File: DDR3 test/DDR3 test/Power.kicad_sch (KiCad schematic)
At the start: 24 parts, among them U1 MPM3834CGPA-Z, U2 MPM3834CGPA-Z, U4 TPS3106K33DBVR

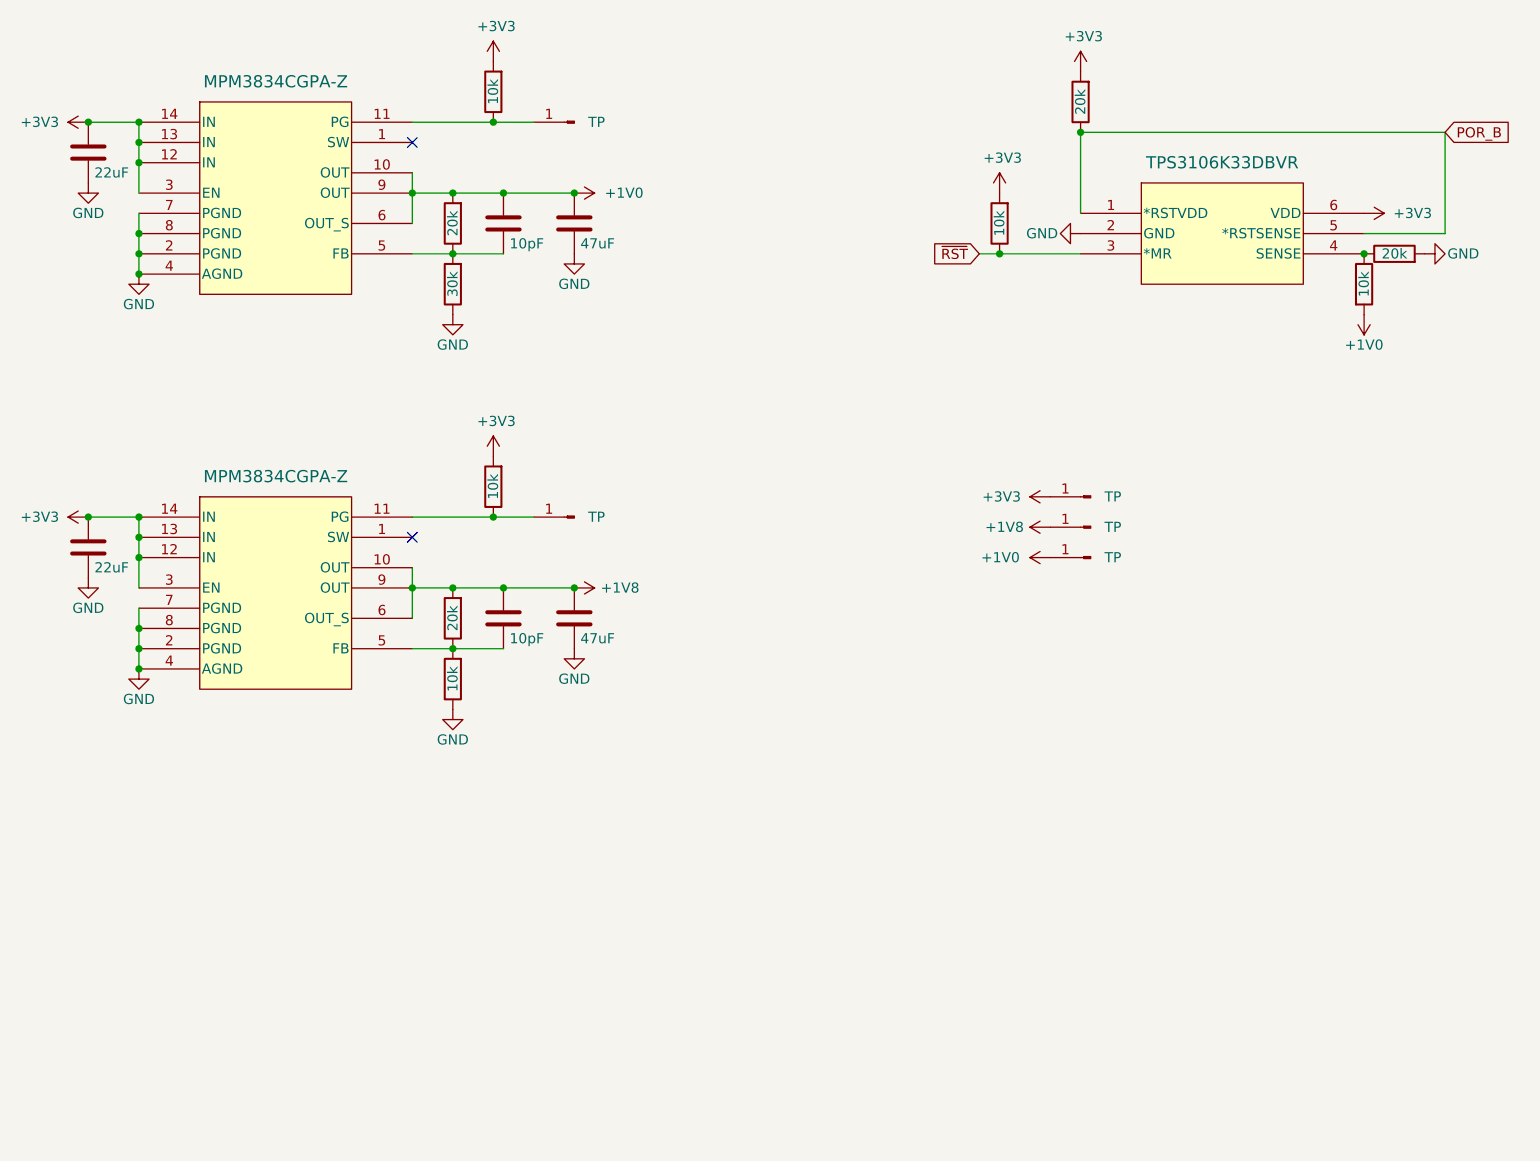
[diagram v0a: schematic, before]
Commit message: group ddr pins by function in symbol
group ddr pins by function in symbol
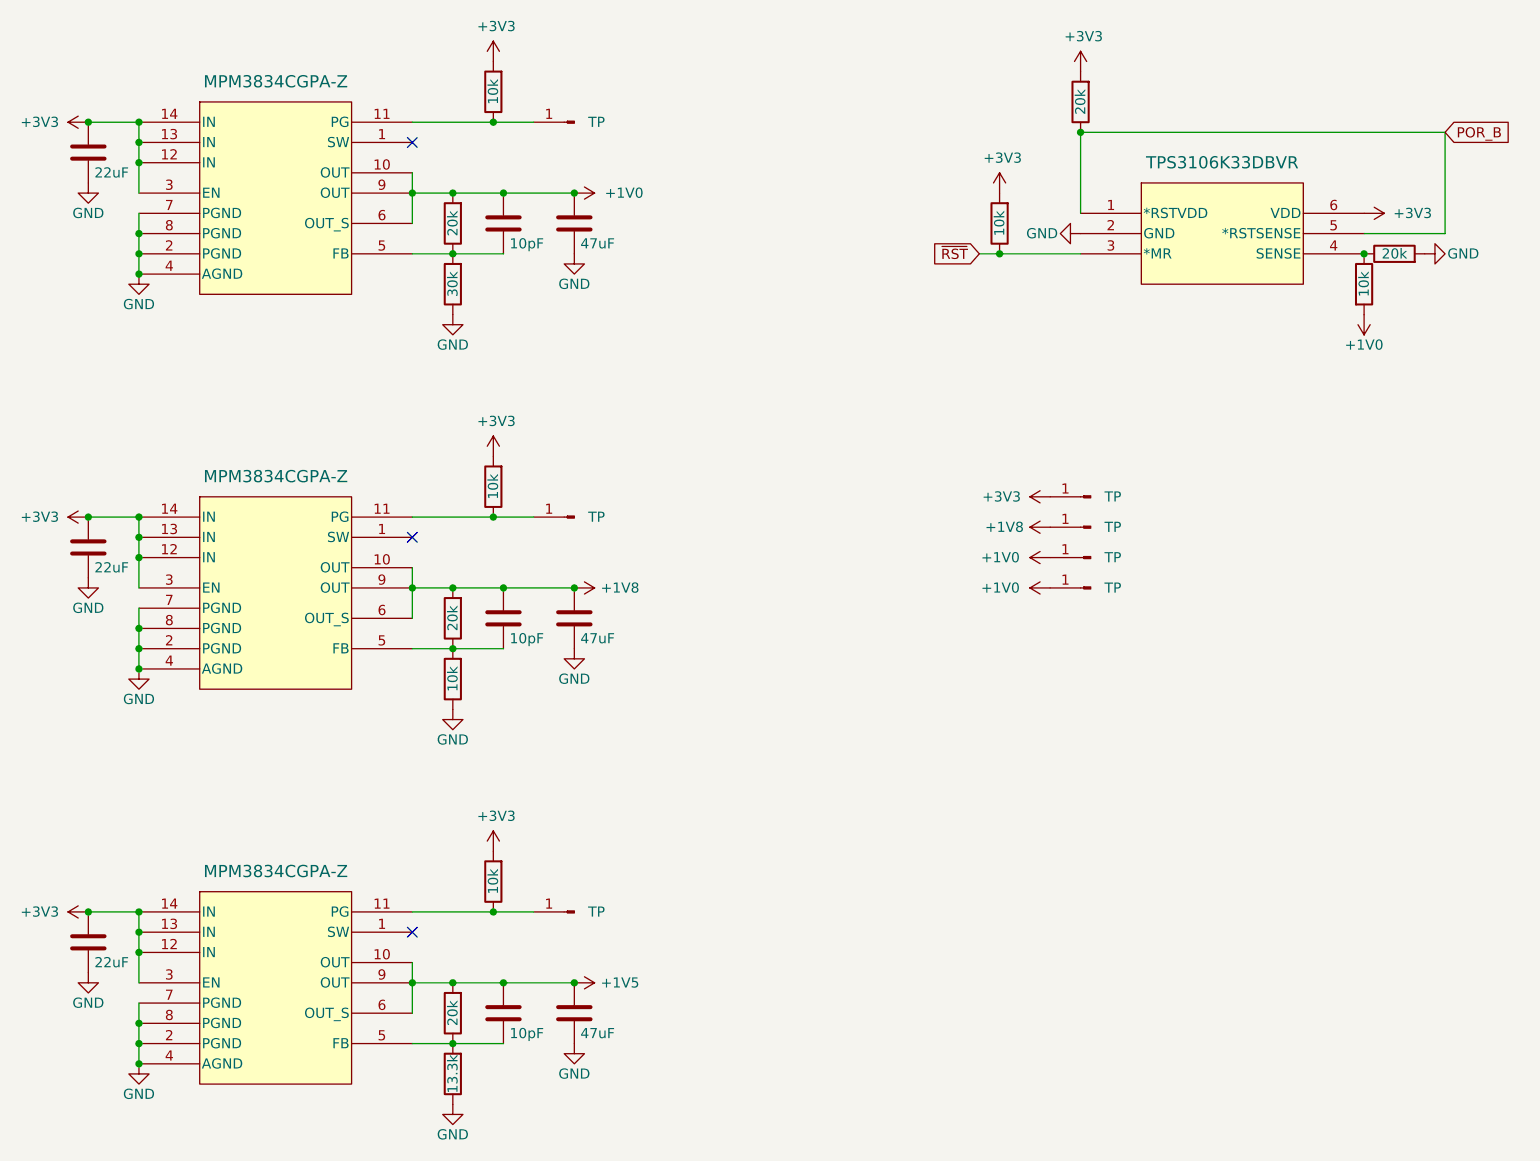
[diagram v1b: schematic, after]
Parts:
- added C2: 22uF, Capacitor_SMD:C_0402_1005Metric, symbol Device:C
- added C3: 10pF, Capacitor_SMD:C_0201_0603Metric, symbol Device:C
- added C4: 47uF, Capacitor_SMD:C_0805_2012Metric, symbol Device:C
- added R29: 20k, Capacitor_SMD:C_0201_0603Metric, symbol Device:R
- added R30: 13.3k, Capacitor_SMD:C_0402_1005Metric, symbol Device:R
- added R31: 10k, Capacitor_SMD:C_0402_1005Metric, symbol Device:R
- added TP6, TP7: TP, TestPoint:TestPoint_Pad_1.0x1.0mm, symbol Connector:Conn_01x01_Pin
- added U8: MPM3834CGPA-Z, Sync_VT extras:ECLGA-14_MPM3834C_MNP, symbol Personal:MPM3834CGPA-Z
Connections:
- net +1V0: now also TP7.1 (Pin_1)
- net +3V3: now also C2.1, R31.2, U8.12 (IN), U8.13 (IN), U8.14 (IN), U8.3 (EN)
- net GND: now also C2.2, C4.2, R30.1, U8.2 (PGND), U8.4 (AGND), U8.7 (PGND), U8.8 (PGND)
- new net: C3.2, R29.1, R30.2, U8.5 (FB)
- new net: R31.1, TP6.1 (Pin_1), U8.11 (PG)
- new net +1V5: C3.1, C4.1, R29.2, U8.10 (OUT), U8.6 (OUT_S), U8.9 (OUT)
- no-connect marks 2 -> 3

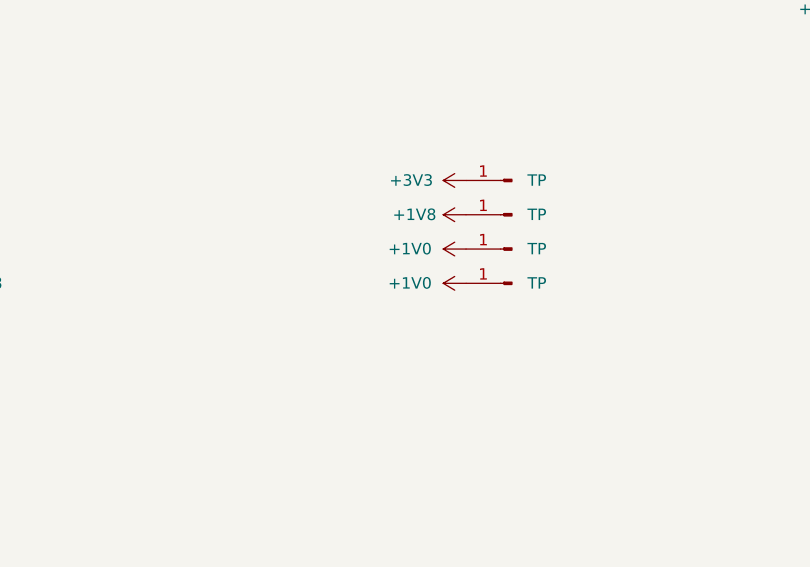
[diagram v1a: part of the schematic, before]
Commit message: Resistor Footprints
- Fixed resistor footprints
- Re-added 3D models
- Routed 1.5V reg
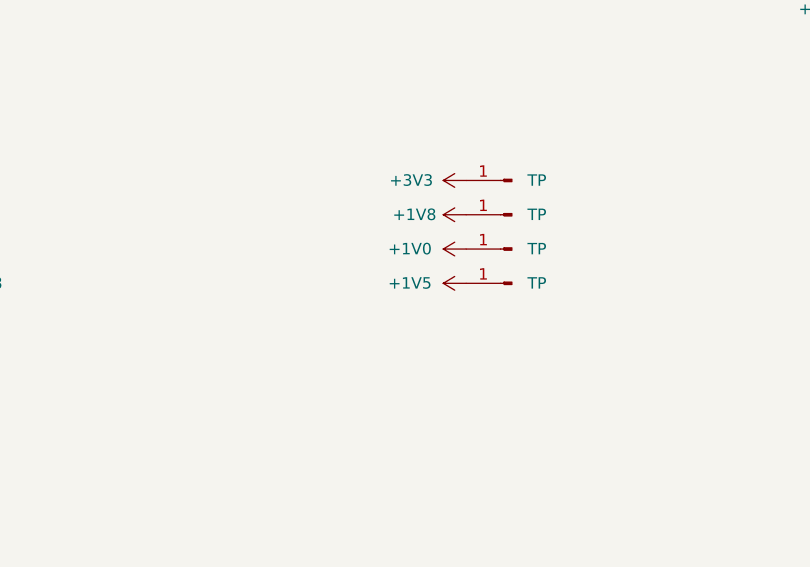
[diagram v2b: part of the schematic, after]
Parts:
- R1, R10, R29, R3, R8: footprint Capacitor_SMD:C_0201_0603Metric -> Resistor_SMD:R_0201_0603Metric
- R2, R30, R31, R4, R5, R6, R7, R9: footprint Capacitor_SMD:C_0402_1005Metric -> Resistor_SMD:R_0402_1005Metric
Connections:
- net +1V0: no longer TP7.1 (Pin_1)
- net +1V5: now also TP7.1 (Pin_1)
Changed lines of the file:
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@@
 			)
 		)
-		(property "Footprint" "Capacitor_SMD:C_0201_0603Metric"
+		(property "Footprint" "Resistor_SMD:R_0201_0603Metric"
 			(at 177.038 40.64 90)
 			(effects
@@
 			)
 		)
-		(property "Footprint" "Capacitor_SMD:C_0402_1005Metric"
+		(property "Footprint" "Resistor_SMD:R_0402_1005Metric"
 			(at 103.378 39.37 90)
 			(effects
@@
 			)
 		)
-		(property "Footprint" "Capacitor_SMD:C_0402_1005Metric"
+		(property "Footprint" "Resistor_SMD:R_0402_1005Metric"
 			(at 209.042 63.5 90)
 			(effects
@@
 			)
 		)
-		(property "Footprint" "Capacitor_SMD:C_0402_1005Metric"
+		(property "Footprint" "Resistor_SMD:R_0402_1005Metric"
 			(at 103.378 88.9 90)
 			(effects
@@
 			)
 		)
-		(property "Footprint" "Capacitor_SMD:C_0201_0603Metric"
+		(property "Footprint" "Resistor_SMD:R_0201_0603Metric"
 			(at 98.298 55.88 90)
 			(effects
@@
 			)
 		)
-		(property "Footprint" "Capacitor_SMD:C_0201_0603Metric"
+		(property "Footprint" "Resistor_SMD:R_0201_0603Metric"
 			(at 98.298 105.41 90)
 			(effects
@@
 			)
 		)
-		(property "Footprint" "Capacitor_SMD:C_0402_1005Metric"
+		(property "Footprint" "Resistor_SMD:R_0402_1005Metric"
 			(at 98.298 113.03 90)
 			(effects
@@
 			)
 		)
-		(property "Footprint" "Capacitor_SMD:C_0402_1005Metric"
+		(property "Footprint" "Resistor_SMD:R_0402_1005Metric"
 			(at 103.378 138.43 90)
 			(effects
@@
 			)
 		)
-		(property "Footprint" "Capacitor_SMD:C_0402_1005Metric"
+		(property "Footprint" "Resistor_SMD:R_0402_1005Metric"
 			(at 98.298 63.5 90)
 			(effects
@@
 			)
 		)
-		(property "Value" "+1V0"
+		(property "Value" "+1V5"
 			(at 167.64 101.5999 90)
 			(effects
@@
 			)
 		)
-		(property "Footprint" "Capacitor_SMD:C_0402_1005Metric"
+		(property "Footprint" "Resistor_SMD:R_0402_1005Metric"
 			(at 98.298 162.56 90)
 			(effects
@@
 			)
 		)
-		(property "Footprint" "Capacitor_SMD:C_0402_1005Metric"
+		(property "Footprint" "Resistor_SMD:R_0402_1005Metric"
 			(at 166.878 55.88 90)
 			(effects
@@
 			)
 		)
-		(property "Footprint" "Capacitor_SMD:C_0201_0603Metric"
+		(property "Footprint" "Resistor_SMD:R_0201_0603Metric"
 			(at 98.298 154.94 90)
 			(effects
@@
 			)
 		)
-		(property "Footprint" "Capacitor_SMD:C_0201_0603Metric"
+		(property "Footprint" "Resistor_SMD:R_0201_0603Metric"
 			(at 214.63 61.468 90)
 			(effects
